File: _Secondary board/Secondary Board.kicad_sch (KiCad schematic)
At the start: 21 parts, among them IC1 AS5600-ASOT, J2 Anemometer, J3 PINHD_1x5_Male, J5 SENSORS, U1 BME680, U2 VEML7700-TR, U3 HT7533

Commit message: Secondary Board now has the hall sensor interated Fixed BME680 schematic mistakes Updated gitignore
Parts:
- removed C4: 100nF, Capacitor_SMD:C_1206_3216Metric_Pad1.33x1.80mm_HandSolder, symbol PCM_SL_Devices:Capacitor_NP
- removed J2: Anemometer, Connector_JST:JST_EH_B3B-EH-A_1x03_P2.50mm_Vertical, symbol PCM_SL_Connectors:JST_03
- removed J3: PINHD_1x5_Male, Connector_PinHeader_2.54mm:PinHeader_1x05_P2.54mm_Vertical, symbol PCM_SL_Pin_Headers:PINHD_1x5_Male
- removed J5: SENSORS, Connector_RJ:RJ45_Amphenol_RJHSE538X, symbol Connector:RJ45_LED_Shielded
- removed JP1: SolderJumper_2_Bridged, Jumper:SolderJumper-2_P1.3mm_Bridged2Bar_RoundedPad1.0x1.5mm, symbol Jumper:SolderJumper_2_Bridged
- removed R2: 70R, Resistor_SMD:R_1206_3216Metric, symbol Device:R
- removed TP1: TestPoint, TestPoint:TestPoint_Pad_D2.0mm, symbol Connector:TestPoint
- added J1: Conn_01x05_Socket, Connector_Hirose:Hirose_DF13-05P-1.25DSA_1x05_P1.25mm_Vertical, symbol Connector:Conn_01x05_Socket
- added JP2: SolderJumper_3_Open, Jumper:SolderJumper-3_P1.3mm_Open_RoundedPad1.0x1.5mm, symbol Jumper:SolderJumper_3_Open
- added U4: A3144, Package_TO_SOT_THT:TO-92S, symbol Sensor_Magnetic:A1302xUA
- R1: value 150R -> 10K
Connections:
- net +3V3: now also C3.2, U1.2 (CSB), U1.6 (VDDIO), U1.8 (VDD)
- net +5V: now also J1.5 (Pin_5), JP2.3 (B), U4.1 (V_{CC})
- net GND: now also IC1.5 (PGO), J1.4 (Pin_4), JP2.1 (A), U4.2 (GND); no longer R1.2
- net SCL: now also R13.1, J1.1 (Pin_1); no longer R12.1
- net SDA: now also R12.1, J1.2 (Pin_2); no longer R13.1
- net W_SPEED: now also R1.2, J1.3 (Pin_3), U4.3 (V_{OUT})
- net at R1.1: now also JP2.2 (C)
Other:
- note added: "AS5600"
- note added: "Anemometer"
- note added: "GND for Default Address"
- note removed: "AS7700"
- note removed: "Connectors"
- moved on the sheet: C1, C2, C3, R12, R13, U3

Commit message: Properly saved the files
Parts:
- added H3: MountingHole_M3_3.2mm_Pad, MountingHole:MountingHole_2.2mm_M2_DIN965_Pad, symbol PCM_SL_Mechanical:MountingHole_M3_3.2mm_Pad
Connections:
- net GND: now also H3.1
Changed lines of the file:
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@@
-	)
-	(junction
-		(at 86.36 179.07)
-		(diameter 0)
-		(color 0 0 0 0)
 	)
 	(junction
@@
 	)
 	(junction
+		(at 81.28 179.07)
+		(diameter 0)
+		(color 0 0 0 0)
+	)
+	(junction
 		(at 82.55 53.34)
 		(diameter 0)
@@
 	(wire
 		(pts
-			(xy 81.28 179.07) (xy 86.36 179.07)
-		)
-		(stroke
-			(width 0)
-			(type default)
-		)
-	)
-	(wire
-		(pts
 			(xy 222.25 125.73) (xy 222.25 124.46)
 		)
@@
 	(wire
 		(pts
+			(xy 81.28 179.07) (xy 92.71 179.07)
+		)
+		(stroke
+			(width 0)
+			(type default)
+		)
+	)
+	(wire
+		(pts
 			(xy 222.25 124.46) (xy 226.06 124.46)
 		)
@@
 	(wire
 		(pts
+			(xy 69.85 179.07) (xy 81.28 179.07)
+		)
+		(stroke
+			(width 0)
+			(type default)
+		)
+	)
+	(wire
+		(pts
 			(xy 72.39 50.8) (xy 71.12 50.8)
 		)
@@
 		(pts
 			(xy 128.27 121.92) (xy 130.81 121.92)
-		)
-		(stroke
-			(width 0)
-			(type default)
-		)
-	)
-	(wire
-		(pts
-			(xy 86.36 179.07) (xy 92.71 179.07)
 		)
 		(stroke
@@
 	(symbol
 		(lib_id "power:GND")
-		(at 86.36 179.07 0)
+		(at 81.28 179.07 0)
 		(unit 1)
 		(exclude_from_sim no)
@@
 		(dnp no)
 		(property "Reference" "#PWR022"
-			(at 86.36 185.42 0)
+			(at 81.28 185.42 0)
 			(effects
 				(font
@@
 		)
 		(property "Value" "GND"
-			(at 86.36 182.88 0)
+			(at 81.28 182.88 0)
 			(effects
 				(font
@@
 		)
 		(property "Footprint" ""
-			(at 86.36 179.07 0)
+			(at 81.28 179.07 0)
 			(effects
 				(font
@@
 		)
 		(property "Datasheet" ""
-			(at 86.36 179.07 0)
+			(at 81.28 179.07 0)
 			(effects
 				(font
@@
 		)
 		(property "Description" "Power symbol creates a global label with name \"GND\" , ground"
-			(at 86.36 179.07 0)
+			(at 81.28 179.07 0)
 			(effects
 				(font
@@
 					(unit 1)
 				)
+			)
+		)
+	)
+	(symbol
+		(lib_id "PCM_SL_Mechanical:MountingHole_M3_3.2mm_Pad")
+		(at 69.85 173.99 0)
+		(unit 1)
+		(exclude_from_sim no)
+		(in_bom yes)
+		(on_board yes)
+		(dnp no)
+		(fields_autoplaced yes)
+		(property "Reference" "H3"
+			(at 73.66 172.7199 0)
+			(effects
+				(font
+					(size 1.27 1.27)
+				)
+				(justify left)
+			)
+		)
+		(property "Value" "MountingHole_M3_3.2mm_Pad"
+			(at 73.66 175.2599 0)
+			(effects
+				(font
+					(size 1.27 1.27)
+				)
+				(justify left)
+				(hide yes)
+			)
+		)
+		(property "Footprint" "MountingHole:MountingHole_2.2mm_M2_DIN965_Pad"
+			(at 69.85 177.8 0)
+			(effects
+				(font
+					(size 1.27 1.27)
+				)
+				(hide yes)
+			)
+		)
+		(property "Datasheet" ""
+			(at 69.85 173.99 0)
+			(effects
+				(font
+					(size 1.27 1.27)
+				)
+				(hide yes)
+			)
+		)
+		(property "Description" "3.2mm Diameter Mounting Hole Pad (M3)"
+			(at 69.85 173.99 0)
+			(effects
+				(font
+					(size 1.27 1.27)
+				)
+				(hide yes)
+			)
+		)
+		(pin "1"
+		)
+		(instances
+			(project "Secondary Board"
+				(path "/148b448d-b722-497b-94de-5b72fb78c9d0"
+					(reference "H3")
+					(unit 1)
+				)

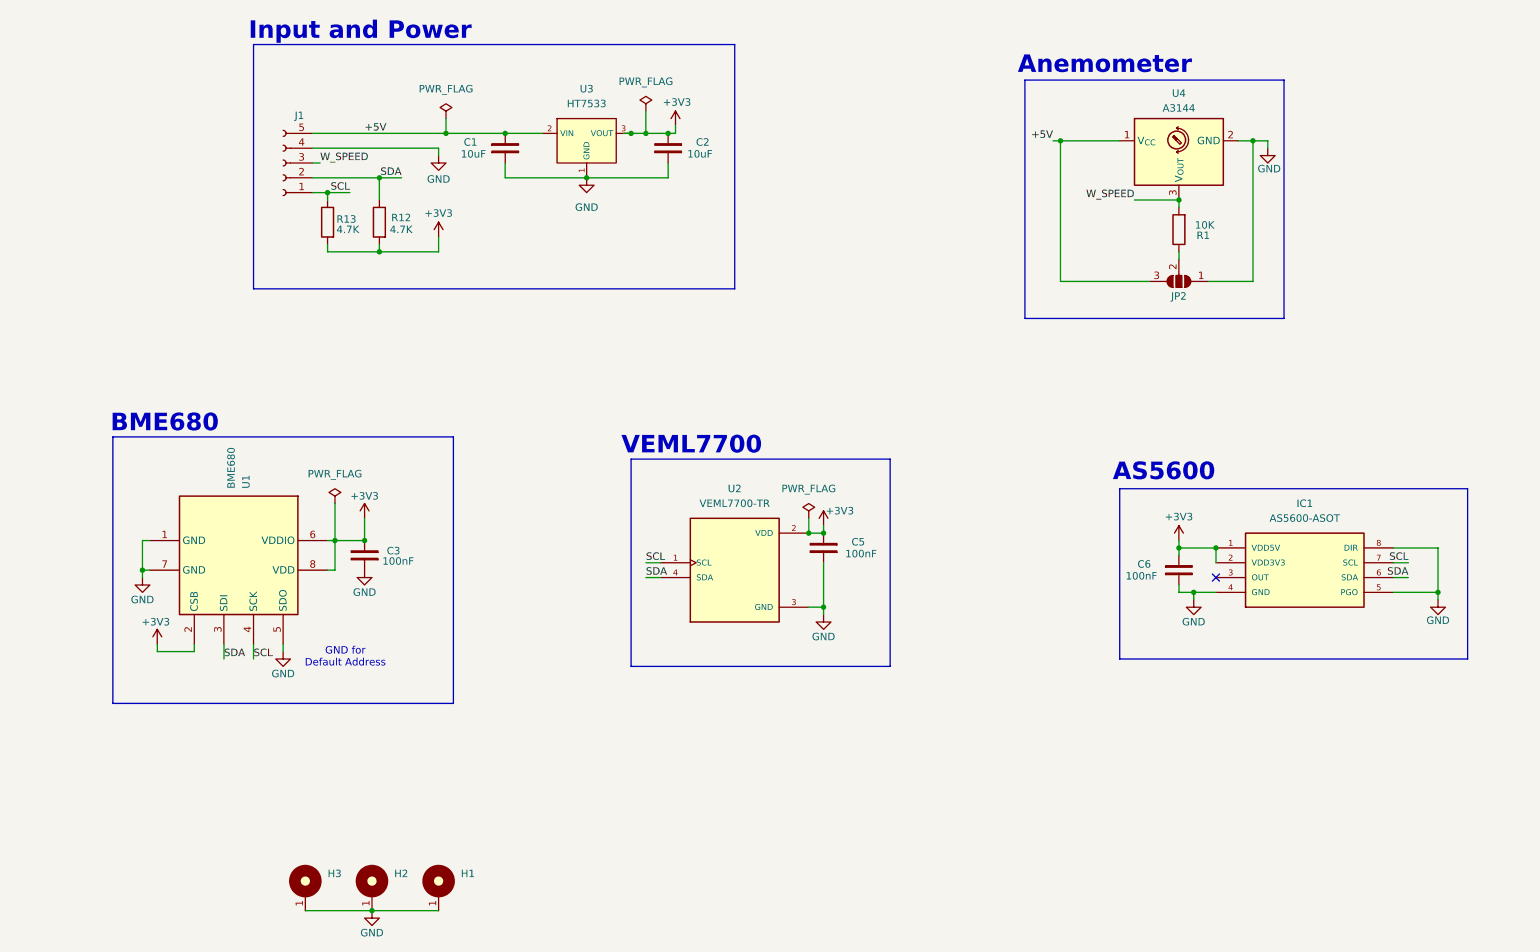
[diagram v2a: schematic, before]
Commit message: Replaced BME680 with BME280 Added Testpoints
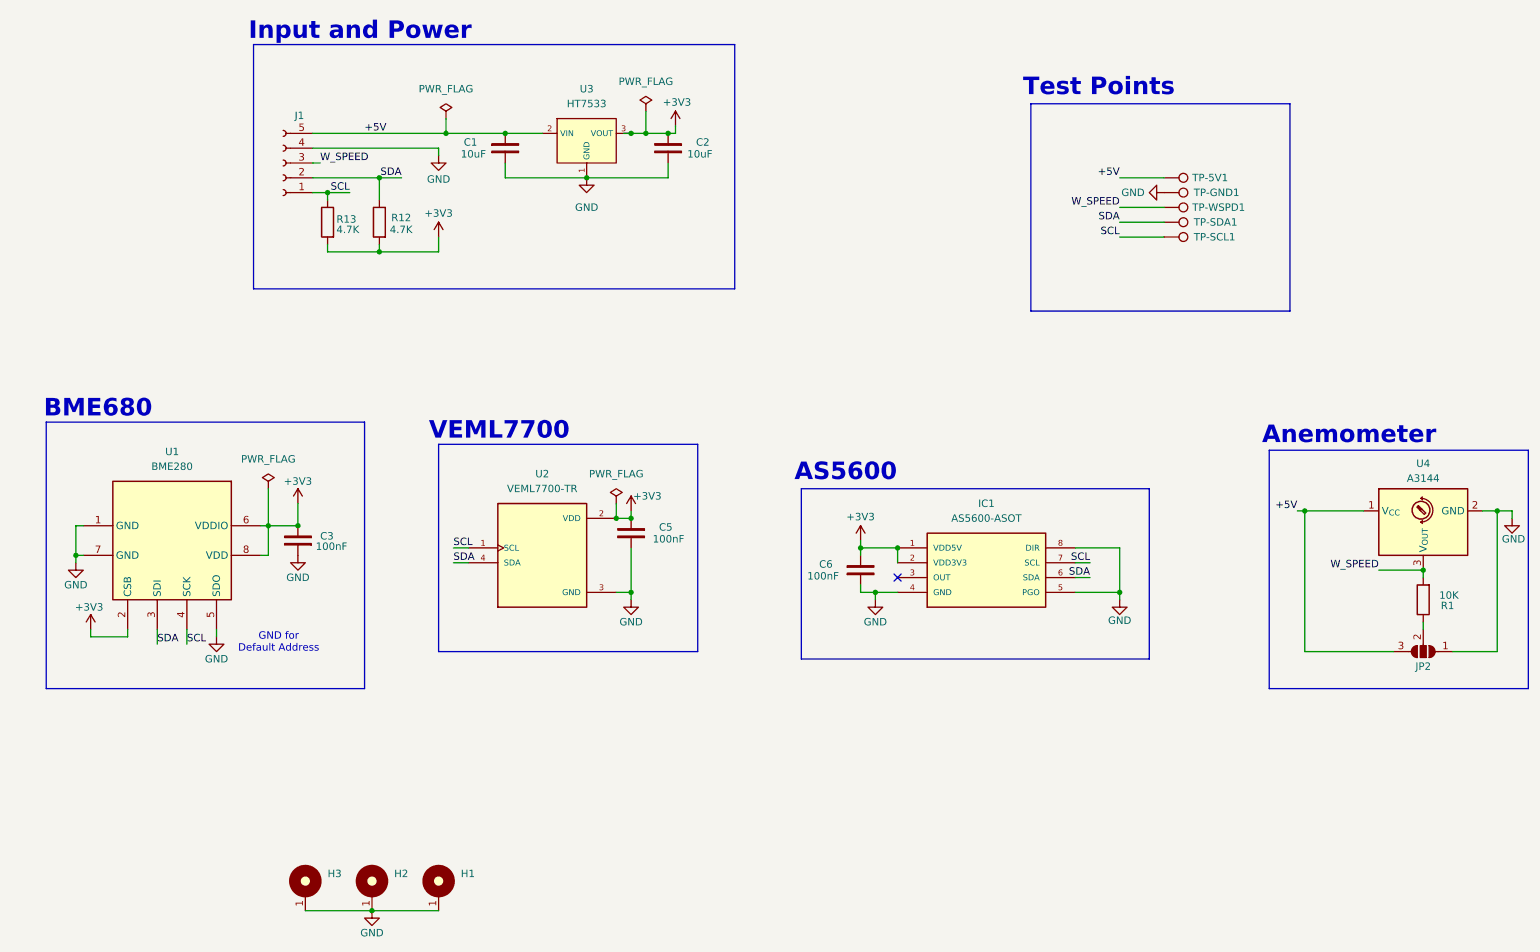
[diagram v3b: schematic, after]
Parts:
- removed U1: BME680, Package_LGA:Bosch_LGA-8_3x3mm_P0.8mm_ClockwisePinNumbering, symbol Sensor:BME680
- added TP-5V1, TP-GND1, TP-SCL1, TP-SDA1, TP-WSPD1: TestPoint, TestPoint:TestPoint_THTPad_D1.5mm_Drill0.7mm, symbol Connector:TestPoint
- added U1: BME280, Package_LGA:Bosch_LGA-8_2.5x2.5mm_P0.65mm_ClockwisePinNumbering, symbol Sensor:BME280
- H1, H2, H3: footprint MountingHole:MountingHole_2.2mm_M2_DIN965_Pad -> MountingHole:MountingHole_3.2mm_M3_ISO7380_Pad
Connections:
- net +3V3: now also U1.2 (CSB), U1.6 (VDDIO), U1.8 (VDD)
- net +5V: now also TP-5V1.1
- net GND: now also TP-GND1.1, U1.1 (GND), U1.5 (SDO), U1.7 (GND)
- net SCL: now also TP-SCL1.1, U1.4 (SCK)
- net SDA: now also TP-SDA1.1, U1.3 (SDI)
- net W_SPEED: now also TP-WSPD1.1
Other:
- note added: "Test Points"
- moved on the sheet: C3, C5, C6, IC1, JP2, R1, U2, U4

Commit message: Updated to KiCAD 10.0 Final Commit before JCLPCB Order
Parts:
- IC1: DESCRIPTION Board Mount Hall Effect / Magnetic Sensors AS5600 Magnetic 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 -> (none)
